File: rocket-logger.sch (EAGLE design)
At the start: 61 parts, among them IC1 CC430F513X, U1 MAX1555, X1 0896BM15A0001, X2 USB-MICROB, X3 SMA-142-0701-801/806

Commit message: routing
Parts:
- added C26: (no value), resistor:C-EUC0402
- added L1: (no value), wuerth-elektronik:WE-MK_0603
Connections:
- new net N$23: IC1.TEST, SV1.4
- new net N$26: IC1.RST, SV1.3
- new net N$28: IC1.P2.1, S4.2
- net +3V3: now also L1.2
- net AVCC_RF2: now also L1.1
- net GND: now also C26.1, LED1.C, LED2.C; no longer R2.2, R3.2
- net N$10: now also LED2.A, R3.2; no longer LED2.C, R3.1
- net N$16: now also R2.1; no longer LED1.A
- net N$17: now also R3.1; no longer LED2.A
- net N$2: now also C26.2
- net N$9: now also LED1.A, R2.2; no longer LED1.C, R2.1
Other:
- moved on the sheet: LED1, LED2, R2, R3, S4, SV1
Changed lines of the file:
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@@
 <?xml version="1.0" encoding="utf-8"?>
 <!DOCTYPE eagle SYSTEM "eagle.dtd">
-<eagle version="6.4">
+<eagle version="6.2">
 <drawing>
 <settings>
@@
 <part name="R2" library="rcl" deviceset="R-EU_" device="R0402"/>
 <part name="R3" library="rcl" deviceset="R-EU_" device="R0402"/>
-<part name="GND23" library="supply1" deviceset="GND" device=""/>
-<part name="GND24" library="supply1" deviceset="GND" device=""/>
 <part name="C15" library="resistor" deviceset="C-EU" device="C0402" value="10u"/>
 <part name="C16" library="resistor" deviceset="C-EU" device="C0402" value="100n"/>
@@
 <part name="+3V12" library="supply1" deviceset="+3V3" device=""/>
 <part name="GND45" library="SparkFun" deviceset="GND" device=""/>
+<part name="C26" library="resistor" deviceset="C-EU" device="C0402"/>
+<part name="GND46" library="SparkFun" deviceset="GND" device=""/>
+<part name="GND23" library="supply1" deviceset="GND" device=""/>
+<part name="GND24" library="supply1" deviceset="GND" device=""/>
+<part name="L1" library="wuerth-elektronik" deviceset="WE-MK" device="_0603"/>
 </parts>
 <sheets>
@@
 <instance part="X1" gate="G$1" x="-29.21" y="170.18" rot="MR0"/>
 <instance part="U1" gate="G$1" x="124.46" y="226.06"/>
-<instance part="LED1" gate="G$1" x="86.36" y="149.86" rot="R90"/>
-<instance part="LED2" gate="G$1" x="86.36" y="147.32" rot="R90"/>
+<instance part="LED1" gate="G$1" x="100.33" y="149.86" rot="R90"/>
+<instance part="LED2" gate="G$1" x="100.33" y="146.05" rot="R90"/>
 <instance part="IC2" gate="G$1" x="165.1" y="220.98"/>
 <instance part="C1" gate="G$1" x="48.26" y="195.58" rot="R270"/>
@@
 <instance part="X3" gate="G1" x="-49.53" y="172.72"/>
 <instance part="GND22" gate="1" x="-46.99" y="167.64"/>
-<instance part="SV1" gate="1" x="-22.86" y="128.27"/>
-<instance part="R2" gate="G$1" x="96.52" y="149.86"/>
-<instance part="R3" gate="G$1" x="96.52" y="147.32"/>
-<instance part="GND23" gate="1" x="104.14" y="147.32" rot="R90"/>
-<instance part="GND24" gate="1" x="104.14" y="149.86" rot="R90"/>
+<instance part="SV1" gate="1" x="-22.86" y="115.57"/>
+<instance part="R2" gate="G$1" x="92.71" y="149.86"/>
+<instance part="R3" gate="G$1" x="92.71" y="146.05"/>
 <instance part="C15" gate="G$1" x="231.14" y="182.88" rot="MR270"/>
 <instance part="C16" gate="G$1" x="227.33" y="187.96" rot="MR270"/>
@@
 <instance part="U$6" gate="G$1" x="176.53" y="128.27"/>
 <instance part="SG1" gate="G$1" x="121.92" y="113.03"/>
-<instance part="S4" gate="G$1" x="87.63" y="189.23"/>
+<instance part="S4" gate="G$1" x="88.9" y="171.45" rot="R180"/>
 <instance part="+3V12" gate="G$1" x="194.31" y="130.81" rot="R270"/>
 <instance part="GND45" gate="1" x="158.75" y="123.19" smashed="yes" rot="R270"/>
+<instance part="C26" gate="G$1" x="139.7" y="233.68" rot="MR0"/>
+<instance part="GND46" gate="1" x="139.7" y="238.76" smashed="yes" rot="R180"/>
+<instance part="GND23" gate="1" x="107.95" y="149.86" rot="R90"/>
+<instance part="GND24" gate="1" x="107.95" y="146.05" rot="R90"/>
+<instance part="L1" gate="G$1" x="26.67" y="196.85"/>
 </instances>
 <busses>
@@
 <wire x1="5.08" y1="198.12" x2="10.16" y2="198.12" width="0.1524" layer="91"/>
 <wire x1="15.24" y1="198.12" x2="20.32" y2="198.12" width="0.1524" layer="91"/>
-<wire x1="20.32" y1="198.12" x2="20.32" y2="200.66" width="0.1524" layer="91"/>
+<wire x1="20.32" y1="198.12" x2="20.32" y2="199.39" width="0.1524" layer="91"/>
 <pinref part="C6" gate="G$1" pin="2"/>
+<wire x1="20.32" y1="199.39" x2="20.32" y2="200.66" width="0.1524" layer="91"/>
 <wire x1="15.24" y1="200.66" x2="15.24" y2="198.12" width="0.1524" layer="91"/>
 <pinref part="C7" gate="G$1" pin="2"/>
@@
 <wire x1="22.86" y1="190.5" x2="22.86" y2="187.96" width="0.1524" layer="91"/>
 <junction x="22.86" y="187.96"/>
+<pinref part="L1" gate="G$1" pin="1"/>
+<wire x1="21.59" y1="199.39" x2="20.32" y2="199.39" width="0.1524" layer="91"/>
+<junction x="20.32" y="199.39"/>
 </segment>
 </net>
@@
 </segment>
 <segment>
-<pinref part="R3" gate="G$1" pin="2"/>
-<pinref part="GND23" gate="1" pin="GND"/>
-</segment>
-<segment>
-<pinref part="R2" gate="G$1" pin="2"/>
-<pinref part="GND24" gate="1" pin="GND"/>
-</segment>
-<segment>
 <pinref part="C15" gate="G$1" pin="1"/>
 <pinref part="GND25" gate="1" pin="GND"/>
@@
 <pinref part="U$6" gate="G$1" pin="GND"/>
 <pinref part="GND45" gate="1" pin="GND"/>
+</segment>
+<segment>
+<pinref part="C26" gate="G$1" pin="1"/>
+<pinref part="GND46" gate="1" pin="GND"/>
+</segment>
+<segment>
+<pinref part="LED1" gate="G$1" pin="C"/>
+<pinref part="GND23" gate="1" pin="GND"/>
+</segment>
+<segment>
+<pinref part="LED2" gate="G$1" pin="C"/>
+<pinref part="GND24" gate="1" pin="GND"/>
 </segment>
 </net>
@@
 <wire x1="140.97" y1="214.63" x2="139.7" y2="214.63" width="0.1524" layer="91"/>
 <junction x="139.7" y="214.63"/>
+<pinref part="C26" gate="G$1" pin="2"/>
 </segment>
 </net>
@@
 <wire x1="45.72" y1="203.2" x2="45.72" y2="200.66" width="0.1524" layer="91"/>
 <wire x1="40.64" y1="200.66" x2="33.02" y2="200.66" width="0.1524" layer="91"/>
-<wire x1="33.02" y1="200.66" x2="33.02" y2="187.96" width="0.1524" layer="91"/>
+<wire x1="33.02" y1="200.66" x2="33.02" y2="199.39" width="0.1524" layer="91"/>
 <junction x="33.02" y="187.96"/>
 <junction x="35.56" y="187.96"/>
@@
 <pinref part="+3V9" gate="G$1" pin="+3V3"/>
 <junction x="33.02" y="200.66"/>
+<pinref part="L1" gate="G$1" pin="2"/>
+<wire x1="33.02" y1="199.39" x2="33.02" y2="187.96" width="0.1524" layer="91"/>
+<wire x1="31.75" y1="199.39" x2="33.02" y2="199.39" width="0.1524" layer="91"/>
+<junction x="33.02" y="199.39"/>
 </segment>
 <segment>
@@
 </segment>
 </net>
-<net name="N$9" class="0">
-<segment>
-<pinref part="LED1" gate="G$1" pin="C"/>
-<pinref part="R2" gate="G$1" pin="1"/>
-</segment>
-</net>
-<net name="N$10" class="0">
-<segment>
-<pinref part="LED2" gate="G$1" pin="C"/>
-<pinref part="R3" gate="G$1" pin="1"/>
-</segment>
-</net>
 <net name="N$13" class="0">
 <segment>
@@
 <net name="N$16" class="0">
 <segment>
-<pinref part="LED1" gate="G$1" pin="A"/>
-<wire x1="83.82" y1="149.86" x2="80.01" y2="149.86" width="0.1524" layer="91"/>
 <wire x1="80.01" y1="149.86" x2="77.47" y2="147.32" width="0.1524" layer="91"/>
 <wire x1="77.47" y1="147.32" x2="77.47" y2="135.89" width="0.1524" layer="91"/>
@@
 <pinref part="IC1" gate="G$1" pin="P3.0"/>
 <wire x1="71.12" y1="129.54" x2="66.04" y2="129.54" width="0.1524" layer="91"/>
+<wire x1="80.01" y1="149.86" x2="87.63" y2="149.86" width="0.1524" layer="91"/>
+<pinref part="R2" gate="G$1" pin="1"/>
 </segment>
 </net>
@@
 <wire x1="66.04" y1="127" x2="72.39" y2="127" width="0.1524" layer="91"/>
 <wire x1="72.39" y1="127" x2="80.01" y2="134.62" width="0.1524" layer="91"/>
-<pinref part="LED2" gate="G$1" pin="A"/>
 <wire x1="80.01" y1="134.62" x2="80.01" y2="143.51" width="0.1524" layer="91"/>
-<wire x1="80.01" y1="143.51" x2="83.82" y2="147.32" width="0.1524" layer="91"/>
+<pinref part="R3" gate="G$1" pin="1"/>
+<wire x1="87.63" y1="146.05" x2="82.55" y2="146.05" width="0.1524" layer="91"/>
+<wire x1="82.55" y1="146.05" x2="80.01" y2="143.51" width="0.1524" layer="91"/>
 </segment>
 </net>
@@
 </segment>
 </net>
+<net name="N$23" class="0">
+<segment>
+<pinref part="IC1" gate="G$1" pin="TEST"/>
+<wire x1="-2.54" y1="119.38" x2="-7.62" y2="119.38" width="0.1524" layer="91"/>
+<pinref part="SV1" gate="1" pin="4"/>
+<wire x1="-15.24" y1="118.11" x2="-7.62" y2="118.11" width="0.1524" layer="91"/>
+<wire x1="-7.62" y1="118.11" x2="-7.62" y2="119.38" width="0.1524" layer="91"/>
+</segment>
+</net>
+<net name="N$26" class="0">
+<segment>
+<pinref part="IC1" gate="G$1" pin="RST"/>
+<wire x1="-15.24" y1="115.57" x2="-2.54" y2="115.57" width="0.1524" layer="91"/>
+<wire x1="-2.54" y1="115.57" x2="-2.54" y2="114.3" width="0.1524" layer="91"/>
+<pinref part="SV1" gate="1" pin="3"/>
+</segment>
+</net>
+<net name="N$9" class="0">
+<segment>
+<pinref part="R2" gate="G$1" pin="2"/>
+<pinref part="LED1" gate="G$1" pin="A"/>
+</segment>
+</net>
+<net name="N$10" class="0">
+<segment>
+<pinref part="R3" gate="G$1" pin="2"/>
+<pinref part="LED2" gate="G$1" pin="A"/>
+</segment>
+</net>
+<net name="N$28" class="0">
+<segment>
+<pinref part="IC1" gate="G$1" pin="P2.1"/>
+<wire x1="66.04" y1="149.86" x2="68.58" y2="149.86" width="0.1524" layer="91"/>
+<wire x1="68.58" y1="149.86" x2="68.58" y2="161.29" width="0.1524" layer="91"/>
+<pinref part="S4" gate="G$1" pin="2"/>
+<wire x1="68.58" y1="161.29" x2="73.66" y2="161.29" width="0.1524" layer="91"/>
+<wire x1="73.66" y1="161.29" x2="83.82" y2="171.45" width="0.1524" layer="91"/>
+</segment>
+</net>

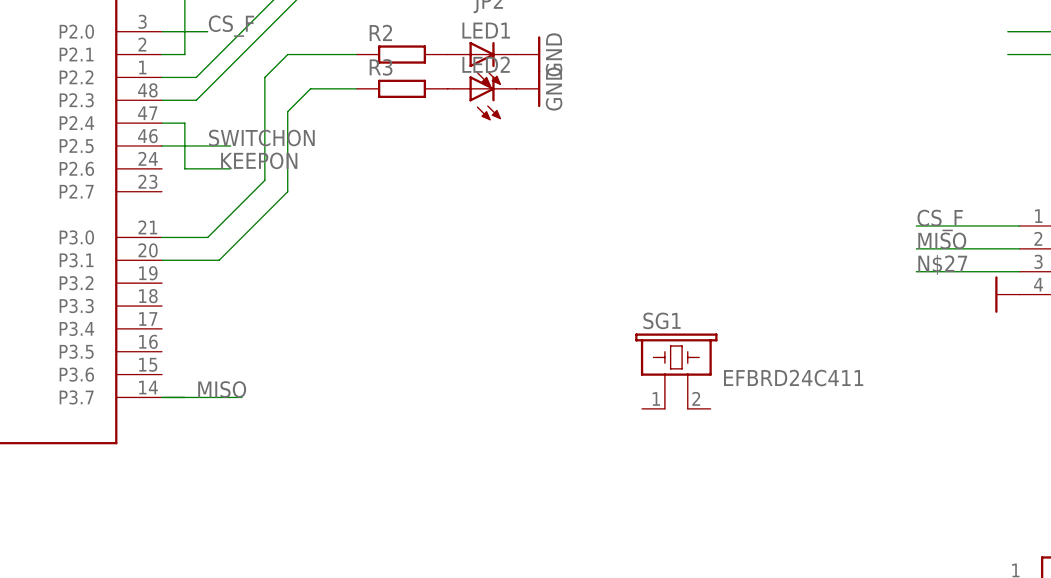
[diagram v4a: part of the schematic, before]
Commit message: wired sounder
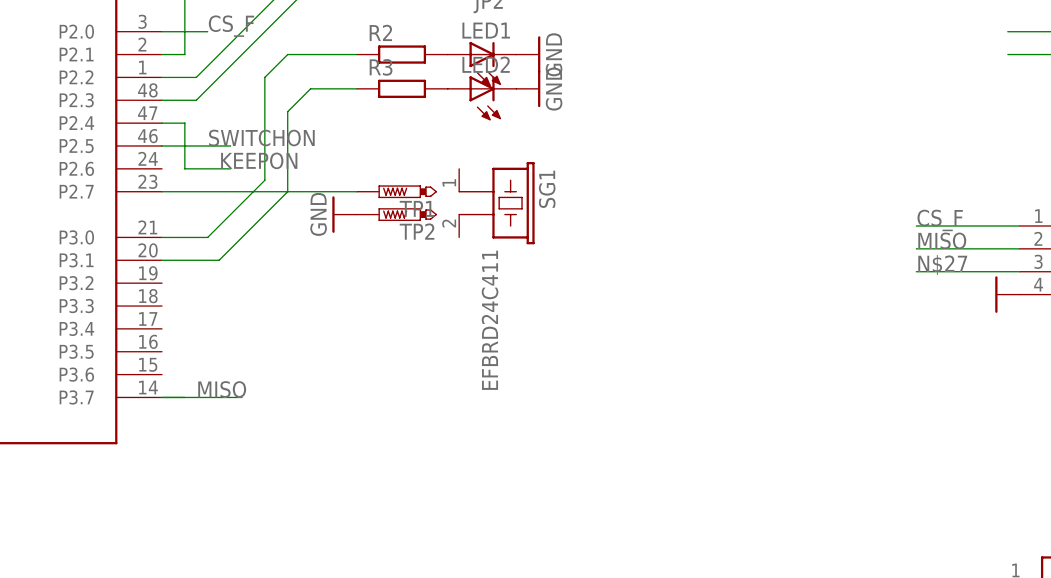
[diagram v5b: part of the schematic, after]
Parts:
- added TP1, TP2: PTR1B1,27, testpad:PTR1B1,27
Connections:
- new net N$29: IC1.P2.7, TP1.TP
- net GND: now also TP2.TP
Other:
- moved on the sheet: SG1
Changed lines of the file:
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@@
 <part name="GND24" library="supply1" deviceset="GND" device=""/>
 <part name="L1" library="wuerth-elektronik" deviceset="WE-MK" device="_0603"/>
+<part name="TP1" library="testpad" deviceset="PTR1" device="B1,27"/>
+<part name="TP2" library="testpad" deviceset="PTR1" device="B1,27"/>
+<part name="GND47" library="supply1" deviceset="GND" device=""/>
 </parts>
 <sheets>
@@
 <instance part="U$5" gate="G$1" x="173.99" y="88.9"/>
 <instance part="U$6" gate="G$1" x="176.53" y="128.27"/>
-<instance part="SG1" gate="G$1" x="121.92" y="113.03"/>
+<instance part="SG1" gate="G$1" x="101.6" y="134.62" rot="R270"/>
 <instance part="S4" gate="G$1" x="88.9" y="171.45" rot="R180"/>
 <instance part="+3V12" gate="G$1" x="194.31" y="130.81" rot="R270"/>
@@
 <instance part="GND24" gate="1" x="107.95" y="146.05" rot="R90"/>
 <instance part="L1" gate="G$1" x="26.67" y="196.85"/>
+<instance part="TP1" gate="G$1" x="90.17" y="134.62" rot="R90"/>
+<instance part="TP2" gate="G$1" x="90.17" y="132.08" rot="R90"/>
+<instance part="GND47" gate="1" x="85.09" y="132.08" rot="R270"/>
 </instances>
 <busses>
@@
 <pinref part="GND24" gate="1" pin="GND"/>
 </segment>
+<segment>
+<pinref part="TP2" gate="G$1" pin="TP"/>
+<pinref part="GND47" gate="1" pin="GND"/>
+</segment>
 </net>
 <net name="N$1" class="0">
@@
 </segment>
 </net>
+<net name="N$29" class="0">
+<segment>
+<pinref part="IC1" gate="G$1" pin="P2.7"/>
+<pinref part="TP1" gate="G$1" pin="TP"/>
+<wire x1="66.04" y1="134.62" x2="87.63" y2="134.62" width="0.1524" layer="91"/>
+</segment>
+</net>
